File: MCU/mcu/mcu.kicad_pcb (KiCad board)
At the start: 2 copper layers, 6 parts, among them U3 ADS8688

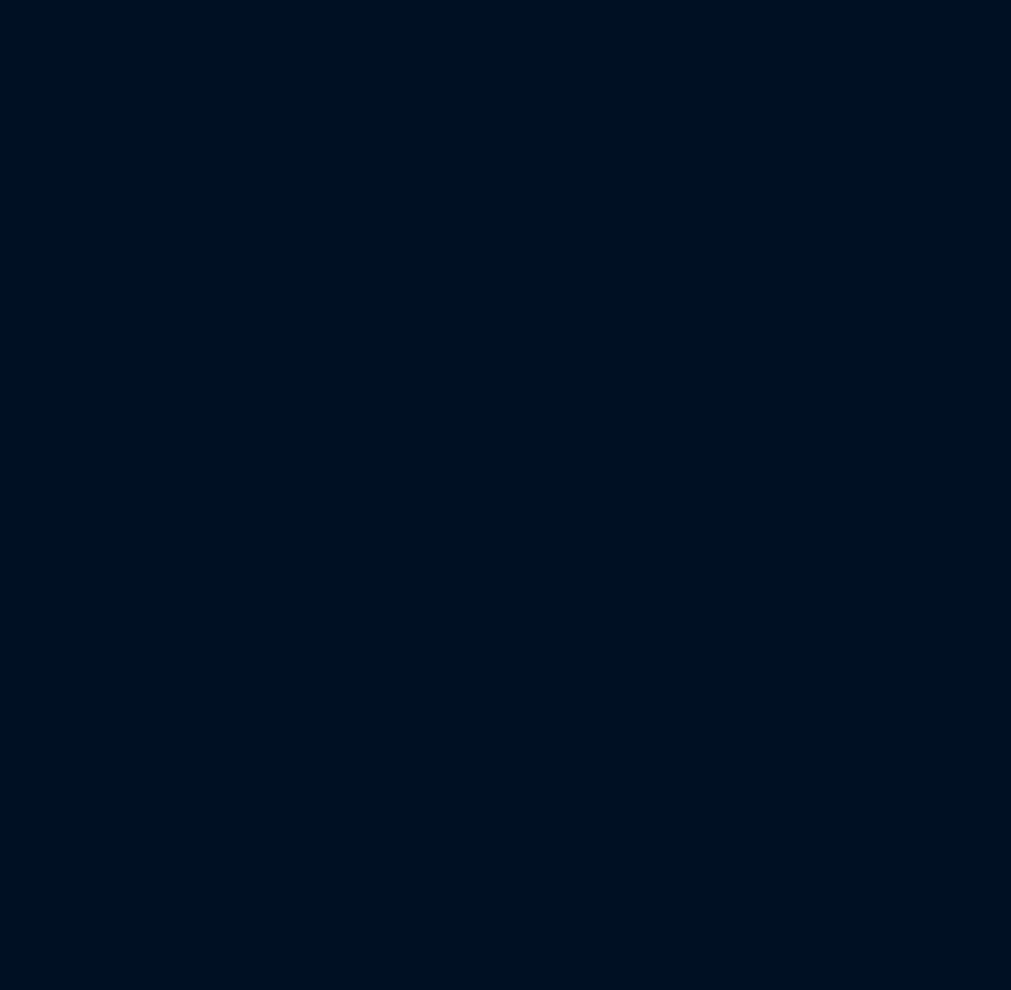
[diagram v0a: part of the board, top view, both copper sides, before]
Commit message: added footprints
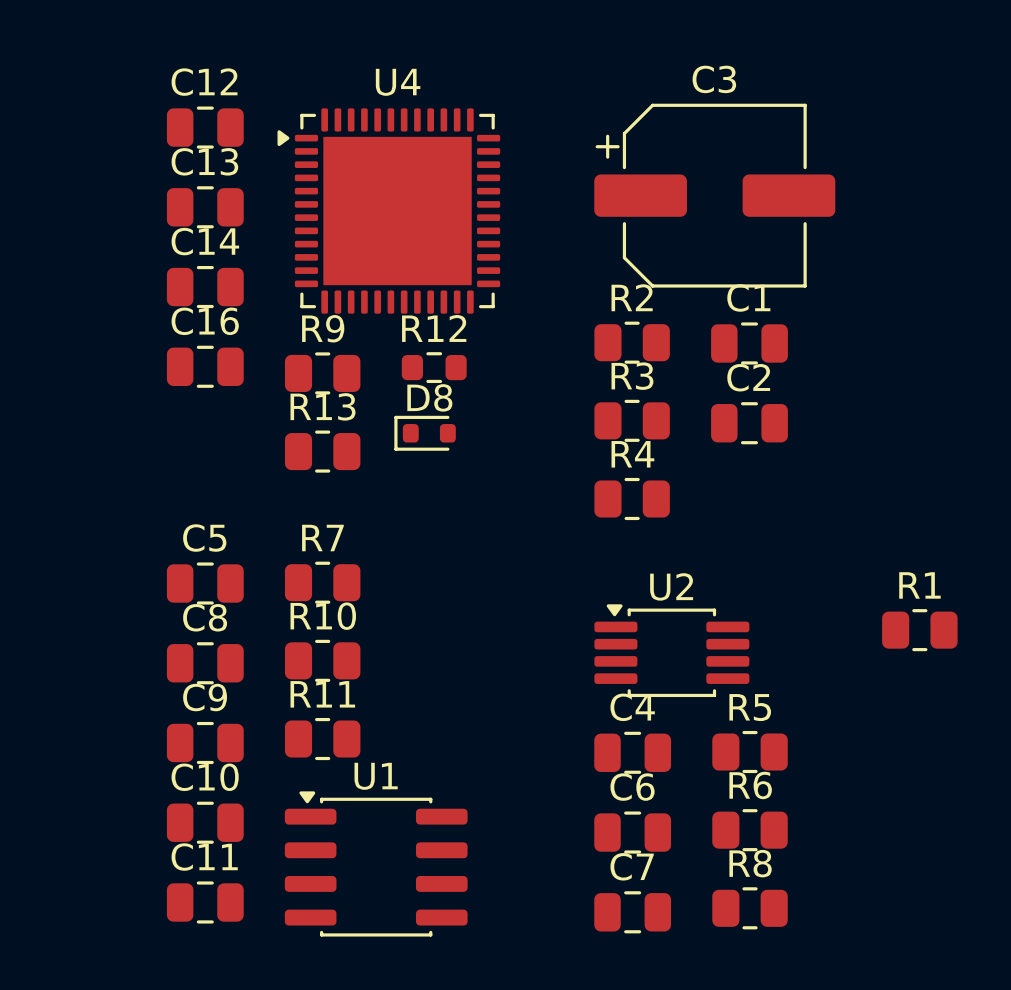
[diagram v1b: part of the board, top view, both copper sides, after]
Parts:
- added C1: 100n, Capacitor_SMD:C_0805_2012Metric, F.Cu at (152.8, 78.2)
- added C10: C, Capacitor_SMD:C_0805_2012Metric, F.Cu at (132.2, 96.2)
- added C11: C, Capacitor_SMD:C_0805_2012Metric, F.Cu at (132.2, 99.3)
- added C12: 1u, Capacitor_SMD:C_0805_2012Metric, F.Cu at (132.2, 70.0)
- added C13: 10u, Capacitor_SMD:C_0805_2012Metric, F.Cu at (132.2, 73.0)
- added C14: 4.7u, Capacitor_SMD:C_0805_2012Metric, F.Cu at (132.2, 76.0)
- added C16: 0.1u, Capacitor_SMD:C_0805_2012Metric, F.Cu at (132.2, 79.0)
- added C2: 10u, Capacitor_SMD:C_0805_2012Metric, F.Cu at (152.8, 81.2)
- added C3: 10u, Capacitor_SMD:CP_Elec_6.3x5.4, F.Cu at (151.5, 72.6)
- added C4: 0.27n, Capacitor_SMD:C_0805_2012Metric, F.Cu at (148.4, 93.6)
- added C5: C, Capacitor_SMD:C_0805_2012Metric, F.Cu at (132.2, 87.2)
- added C6: C, Capacitor_SMD:C_0805_2012Metric, F.Cu at (148.4, 96.6)
- added C7: C, Capacitor_SMD:C_0805_2012Metric, F.Cu at (148.4, 99.6)
- added C8: C, Capacitor_SMD:C_0805_2012Metric, F.Cu at (132.2, 90.2)
- added C9: C, Capacitor_SMD:C_0805_2012Metric, F.Cu at (132.2, 93.2)
- added D8: ESD5Z3.3TiG, Diode_SMD:D_SOD-523, F.Cu at (140.7, 81.5)
- added R1: 33, Resistor_SMD:R_0805_2012Metric, F.Cu at (159.2, 89.0)
- added R10: R, Resistor_SMD:R_0805_2012Metric, F.Cu at (136.7, 90.1)
- added R11: R, Resistor_SMD:R_0805_2012Metric, F.Cu at (136.7, 93.1)
- added R12: 100, Resistor_SMD:R_0603_1608Metric, F.Cu at (140.9, 79.1)
- added R13: 10k, Resistor_SMD:R_0805_2012Metric, F.Cu at (136.7, 82.2)
- added R2: 10k, Resistor_SMD:R_0805_2012Metric, F.Cu at (148.3, 78.1)
- added R3: 10k, Resistor_SMD:R_0805_2012Metric, F.Cu at (148.3, 81.1)
- added R4: 100, Resistor_SMD:R_0805_2012Metric, F.Cu at (148.3, 84.0)
- added R5: 20k, Resistor_SMD:R_0805_2012Metric, F.Cu at (152.8, 93.6)
- added R6: 20k, Resistor_SMD:R_0805_2012Metric, F.Cu at (152.8, 96.5)
- added R7: R, Resistor_SMD:R_0805_2012Metric, F.Cu at (136.7, 87.2)
- added R8: 10k, Resistor_SMD:R_0805_2012Metric, F.Cu at (152.8, 99.5)
- added R9: 10k, Resistor_SMD:R_0805_2012Metric, F.Cu at (136.7, 79.3)
- added U1: INA128, Package_SO:SOIC-8_3.9x4.9mm_P1.27mm, F.Cu at (138.7, 97.9)
- added U2: MCP6002-xMS, Package_SO:MSOP-8_3x3mm_P0.65mm, F.Cu at (149.8, 89.8)
- added U4: STM32F401CCUx, Package_DFN_QFN:QFN-48-1EP_7x7mm_P0.5mm_EP5.6x5.6mm, F.Cu at (139.5, 73.2)
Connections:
- U3 pad 1: unconnected-(U3-SDI-Pad1) -> Net-(U3-SDI)
- U3 pad 2: unconnected-(U3-~{RST/PD}-Pad2) -> Net-(U3-~{RST/PD})
- U3 pad 28: Net-(U3-AGND-Pad28) -> GND
- U3 pad 29: Net-(U3-AGND-Pad28) -> GND
- U3 pad 30: unconnected-(U3-AVDD-Pad30) -> +5V
- U3 pad 31: Net-(U3-AGND-Pad28) -> GND
- U3 pad 32: Net-(U3-AGND-Pad28) -> GND
- U3 pad 33: unconnected-(U3-DGND-Pad33) -> GND
- U3 pad 34: unconnected-(U3-DVDD-Pad34) -> +3.3V
- U3 pad 36: unconnected-(U3-SDO-Pad36) -> Net-(U3-SDO)
- U3 pad 37: unconnected-(U3-SCLK-Pad37) -> Net-(U3-SCLK)
- U3 pad 38: unconnected-(U3-~{CS}-Pad38) -> Net-(U3-~{CS})
- U3 pad 5: unconnected-(U3-REFIO-Pad5) -> Net-(U3-REFIO)
- U3 pad 6: unconnected-(U3-REFGND-Pad6) -> GND
- U3 pad 7: unconnected-(U3-REFCAP-Pad7) -> Net-(U3-REFCAP)
- U3 pad 8: Net-(U3-AGND-Pad28) -> GND
- U3 pad 9: unconnected-(U3-AVDD-Pad9) -> +5V

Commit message: cleaned 3,4
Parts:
- added C11: 100n, Capacitor_SMD:C_01005_0402Metric, F.Cu at (118.6, 99.1)
- added C15: 130p, Capacitor_SMD:C_0805_2012Metric, F.Cu at (113.2, 99.5)
- added C6: 510p, Capacitor_SMD:C_0805_2012Metric, F.Cu at (113.2, 96.5)
- added C7: 100n, Capacitor_SMD:C_01005_0402Metric, F.Cu at (118.6, 95.8)
- added C9: 100n, Capacitor_SMD:C_01005_0402Metric, F.Cu at (118.6, 97.5)
- added T1: SCT-013-000, TerminalBlock:TerminalBlock_MaiXu_MX126-5.0-04P_1x04_P5.00mm, F.Cu at (79.0, 80.5)
- C10: value C -> 1n
- C5, C8: value C -> 100p
- R10, R7: value R -> 2k
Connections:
- C10 pad 1: Net-(C10-Pad1) -> Net-(D3-K)
- C10 pad 2: GND -> Net-(D5-K)
- C8 pad 1: Net-(D3-A) -> Net-(C8-Pad1)
- D3 pad 2: Net-(D3-A) -> -5V
- D4 pad 1: Net-(D3-K) -> +5V
- D4 pad 2: Net-(D3-A) -> Net-(D3-K)
- D5 pad 1: Net-(D3-A) -> Net-(D5-K)
- D5 pad 2: GND -> Net-(D5-A)
- D6 pad 1: Net-(D3-A) -> +5V
- D6 pad 2: GND -> Net-(D5-K)
- R10 pad 2: Net-(D3-A) -> Net-(C8-Pad1)
- R6 pad 2: Net-(U2A--) -> Net-(U2A-+)
- U1 pad 1: Net-(C10-Pad1) -> unconnected-(U1-Rg-Pad1)
- U1 pad 2: Net-(D3-A) -> Net-(D5-K)
- U1 pad 4: GND -> Net-(D5-A)
- U1 pad 5: GND -> Net-(U1-Ref)
- U1 pad 7: VCC -> Net-(U1-V+)
- U1 pad 8: Net-(C10-Pad1) -> unconnected-(U1-Rg-Pad8)
- U2 pad 1: Net-(C6-Pad1) -> Net-(U2B-+)
- U2 pad 2: Net-(U2A--) -> GND
- U2 pad 3: GND -> Net-(U2A-+)
- U2 pad 5: GND -> Net-(U2B-+)
- U2 pad 6: Net-(U2B--) -> /anti_aliasing/Out

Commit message: started pcb design
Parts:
- moved D8 45.9 mm to (103.2, 108.0)
- moved C12 34.4 mm to (166.4, 73.0)
- moved C13 34.4 mm to (166.4, 76.0)
- moved C14 34.4 mm to (166.4, 79.0)
- moved C16 34.4 mm to (166.4, 82.0)
- moved U4 33.3 mm to (164.4, 95.2)
- moved C11 27.6 mm to (143.0, 124.6)
- moved C8 27.6 mm to (143.0, 115.6)
- moved R11 27.6 mm to (147.4, 118.5)
- moved C10 27.6 mm to (143.0, 121.6)
- moved C5 27.6 mm to (143.0, 112.6)
- moved C9 27.6 mm to (143.0, 118.6)
- moved R10 27.6 mm to (147.4, 115.5)
- moved R7 27.6 mm to (147.4, 112.5)
- moved U2 23.0 mm to (127.0, 92.5)
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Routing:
- net (no net): vias 0 -> 1
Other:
- copper layers 2 -> 4

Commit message: h
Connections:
- net /instrumentation_amplifier/Out renamed /instrumentation_amplifier/INA128_Output
- R10 pad 1: /anti_aliasing/Out -> /instrumentation_amplifier/INA128_input
- R7 pad 1: /anti_aliasing/Out -> /instrumentation_amplifier/INA128_input
- U2 pad 6: /anti_aliasing/Out -> /instrumentation_amplifier/INA128_input
- U2 pad 7: /anti_aliasing/Out -> /instrumentation_amplifier/INA128_input
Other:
- board outline added: 104.5 x 67 mm

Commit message: started pcb editing
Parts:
- removed the C11 at (143.0, 124.6)
- removed the C11 at (118.6, 99.1)
- removed the C6 at (134.9, 93.5)
- removed the C6 at (113.2, 96.5)
- removed the C7 at (134.9, 96.5)
- removed the C7 at (118.6, 95.8)
- removed the C9 at (143.0, 118.6)
- removed the C9 at (118.6, 97.5)
- removed R11: R, Resistor_SMD:R_0805_2012Metric
- removed R8: 10k, Resistor_SMD:R_0805_2012Metric
- added C11: 100n, Capacitor_SMD:C_01005_0402Metric, F.Cu at (138.6, 113.7)
- added C6: 510p, Capacitor_SMD:C_0805_2012Metric, F.Cu at (124.5, 121.0)
- added C7: 100n, Capacitor_SMD:C_01005_0402Metric, F.Cu at (138.6, 110.4)
- added C9: 100n, Capacitor_SMD:C_01005_0402Metric, F.Cu at (138.6, 112.0)
- moved C12 61.4 mm to (105.7, 82.0)
- moved C13 61.4 mm to (105.7, 85.0)
- moved C14 61.4 mm to (105.7, 88.0)
- moved C16 61.4 mm to (105.7, 91.0)
- moved U4 51.5 mm to (113.0, 96.6)
- moved C1 49.3 mm to (110.1, 112.9)
- moved C2 49.3 mm to (110.1, 115.9)
- moved C3 49.3 mm to (108.8, 107.3)
- moved R2 49.3 mm to (105.7, 112.9)
- moved R3 49.3 mm to (105.7, 115.8)
- moved R4 49.3 mm to (105.7, 118.8)
- moved T1 47.6 mm to (126.3, 85.5)
- moved R12 38.0 mm to (105.5, 99.7)
- moved R5 33.8 mm to (128.9, 122.6)
- moved R6 33.8 mm to (128.9, 125.5)
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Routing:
- net GND: track 0.00 -> 151.2 mm, vias 0 -> 2
- net /DC_Bias/In: track 0.00 -> 78.7 mm, vias 0 -> 1
- net VCC: track 0.00 -> 70.6 mm, vias 0 -> 2
- net Net-(U3-SDO): track 0.00 -> 57.1 mm
- net Net-(U3-SCLK): track 0.00 -> 35.9 mm
- net Net-(D5-K): track 0.00 -> 35.5 mm
- net +5V: track 0.00 -> 30.1 mm
- net Net-(U3-~{CS}): track 0.00 -> 27.2 mm
- net Net-(D3-K): track 0.00 -> 26.8 mm
- net /DC_Bias/Out: track 0.00 -> 23.0 mm
- net Net-(U2B-+): track 0.00 -> 22.8 mm, vias 0 -> 2
- net /instrumentation_amplifier/INA128_input: track 0.00 -> 21.4 mm
- net -5V: track 0.00 -> 18.4 mm
- net Net-(C1-Pad1): track 0.00 -> 18.0 mm
- net Net-(C4-Pad1): track 0.00 -> 11.9 mm
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
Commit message: completed pcb routing
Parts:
- moved C1 2.55 mm to (107.6, 113.4)
- moved C10 2.55 mm to (132.8, 111.7)
- moved C11 2.55 mm to (136.1, 114.2)
- moved C12 2.55 mm to (103.2, 82.5)
- moved C13 2.55 mm to (103.2, 85.5)
- moved C14 2.55 mm to (103.2, 88.5)
- moved C15 2.55 mm to (122.0, 124.5)
- moved C16 2.55 mm to (103.2, 91.5)
- moved C2 2.55 mm to (107.6, 116.4)
- moved C3 2.55 mm to (106.3, 107.8)
- moved C4 2.55 mm to (122.0, 118.5)
- moved C5 2.55 mm to (132.8, 105.6)
- moved C6 2.55 mm to (122.0, 121.5)
- moved C7 2.55 mm to (136.1, 110.9)
- moved C8 2.55 mm to (132.8, 108.7)
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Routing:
- net GND: track 151.2 -> 215.5 mm
- net /instrumentation_amplifier/INA128_Output: track 0.00 -> 39.9 mm, vias 2 -> 0
- net Net-(U3-SCLK): track 35.9 -> 0.00 mm
- net Net-(U3-SDO): track 57.1 -> 21.3 mm, vias 0 -> 2
- net +3.3V: track 0.00 -> 34.1 mm, vias 0 -> 2
- net Net-(D8-K): track 0.00 -> 33.0 mm, vias 0 -> 3
- net Net-(U3-SDI): track 0.00 -> 27.6 mm, vias 0 -> 2
- net Net-(U4-VCAP1): track 0.00 -> 25.2 mm
- net /DC_Bias/In: track 78.7 -> 53.9 mm, vias 1 -> 2
- net Net-(U3-~{RST/PD}): track 0.00 -> 21.1 mm, vias 0 -> 2
- net -5V: track 18.4 -> 0.00 mm
- net Net-(U4-NRST): track 2.98 -> 13.2 mm
- net Net-(U4-BOOT0): track 8.25 -> 0.00 mm, vias 1 -> 0
- net Net-(C8-Pad1): track 0.00 -> 7.22 mm
- net Net-(D5-K): track 35.5 -> 28.8 mm, vias 0 -> 1
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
